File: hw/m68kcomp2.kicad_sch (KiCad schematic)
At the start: 61 parts, among them U10 as6c8008, U11 mc68681, U12 as6c8008, U13 mc1489, U14 mc1488, U15 mc1488, U16 as6c8008, U17 sera, U18 serb, U2 74HC393, U3 74HC10, U4 74HC148, U5 mc68030rc, U6 28C256, U7 mc68881, U8 as6c8008, U9 GAL16V8, X1 25.175MHz, Y1 3.6864MHz

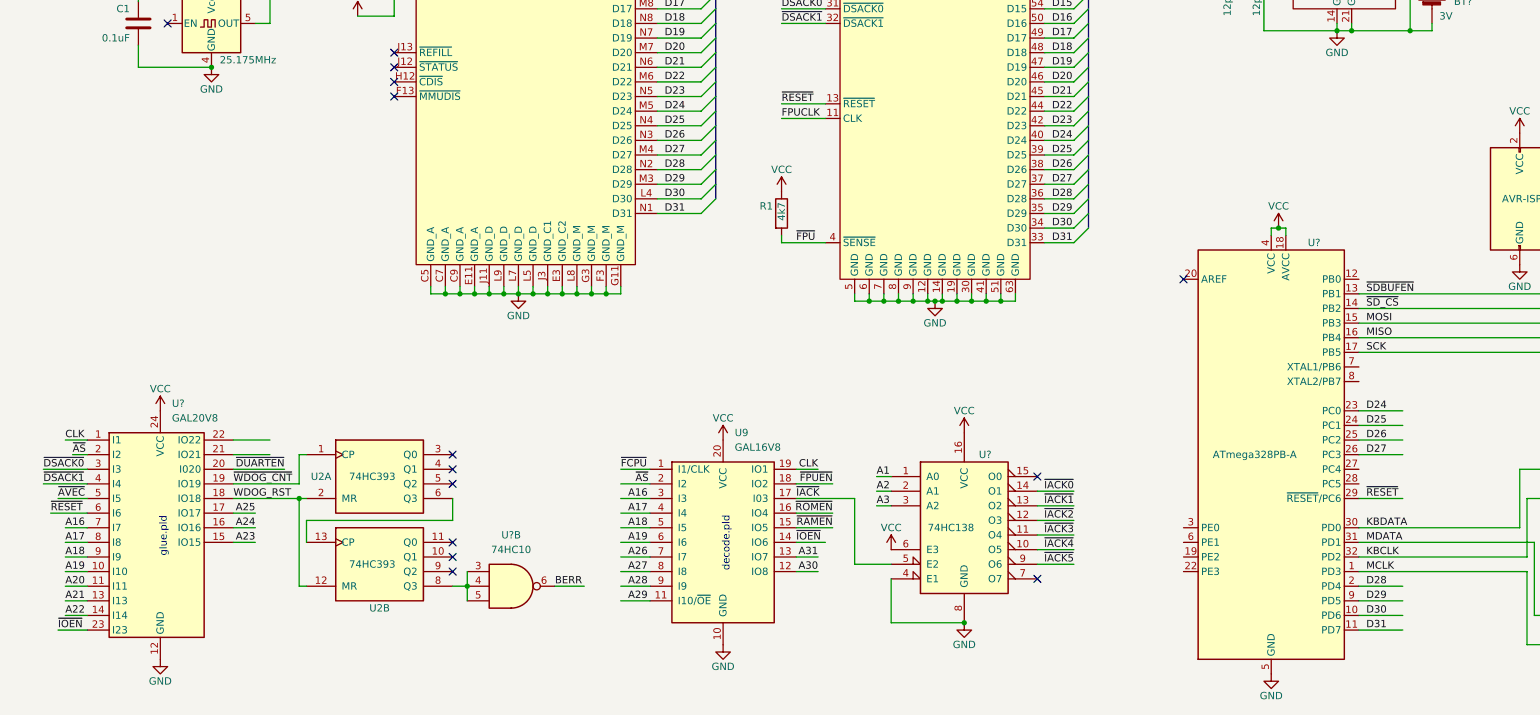
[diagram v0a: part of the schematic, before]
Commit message: schematic progress, split iodecode from glue.pld...
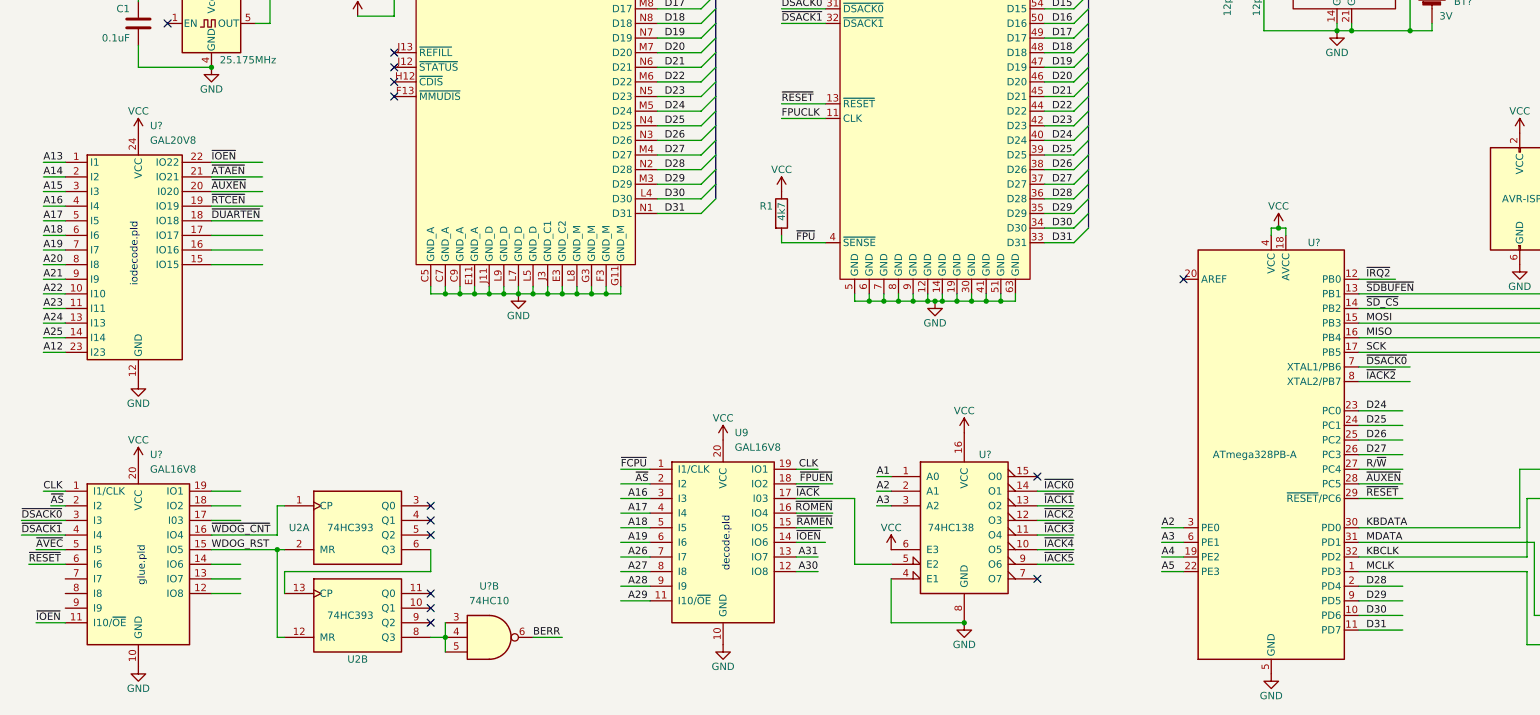
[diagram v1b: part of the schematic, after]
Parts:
- removed U?: GAL20V8, symbol m68kcomp2:GAL20V8
- added U?: GAL20V8, symbol m68kcomp2:GAL20V8
- added U?: GAL16V8, Package_DIP:DIP-20_W7.62mm_Socket, symbol Logic_Programmable:GAL16V8
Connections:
- net A12: now also U?.23 (I23)
- net A13: now also U?.1 (I1)
- net A14: now also U?.2 (I2)
- net A15: now also U?.3 (I3)
- net A16: now also U?.4 (I4)
- net A17: now also U?.5 (I5)
- net A18: now also U?.6 (I6)
- net A19: now also U?.7 (I7)
- net A2: now also U?.3 (PE0)
- net A20: now also U?.8 (I8)
- net A21: now also U?.9 (I9)
- net A22: now also U?.10 (I10)
- net A23: now also U?.11 (I11)
- net A24: now also U?.13 (I13)
- net A25: now also U?.14 (I14)
- net A3: now also U?.6 (PE1)
- net A4: now also U?.19 (PE2)
- net A5: now also U?.22 (PE3)
- net CLK: now also U?.1 (I1/CLK)
- net GND: now also U?.10 (GND), U?.12 (GND)
- net R/~{W}: now also U?.27 (PC4)
- net VCC: now also U?.20 (VCC), U?.24 (VCC)
- net WDOG_RST: now also U?.15 (IO5)
- net ~{AS}: now also U?.2 (I2)
- net ~{AVEC}: now also U?.5 (I5)
- net ~{DSACK0}: now also U?.7 (XTAL1/PB6), U?.3 (I3)
- net ~{DSACK1}: now also U?.4 (I4)
- net ~{DUARTEN}: now also U?.18 (IO18)
- net ~{IACK2}: now also U?.8 (XTAL2/PB7)
- net ~{IOEN}: now also U?.11 (I10/~{OE}), U?.22 (IO22)
- net ~{IRQ2}: now also U?.12 (PB0)
- net ~{RESET}: now also U?.6 (I6)
- net ~{RTCEN}: now also U?.19 (IO19)
- net ~{WDOG_CNT}: now also U?.16 (IO4)
- net ~{AUXEN}: now reaches U?.28 (PC5)
- net ~{AUXEN}: now also U?.20 (I020)
- new net ~{ATAEN}: U?.21 (IO21)
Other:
- note added: "iodecode.pld"
- moved on the sheet: U2A, U2B, U?B

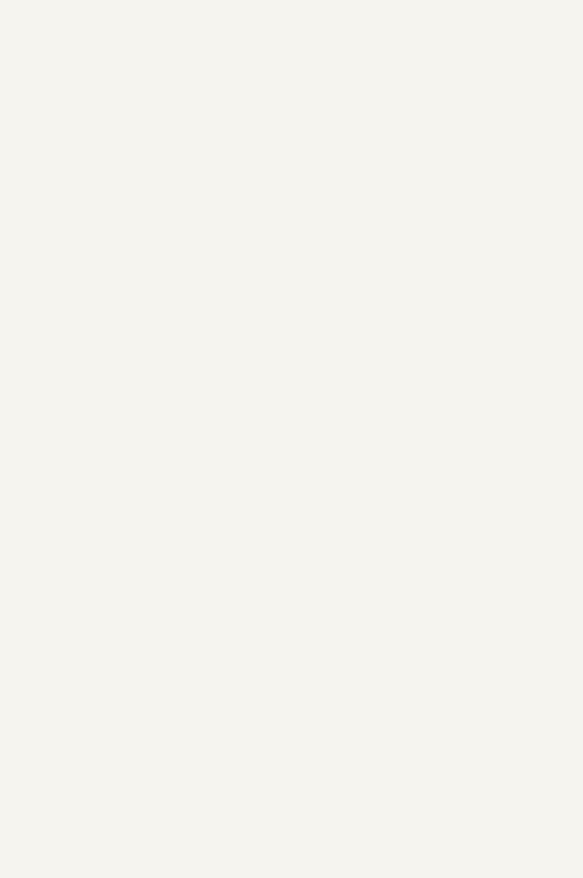
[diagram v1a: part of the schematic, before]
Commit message: ATA connector
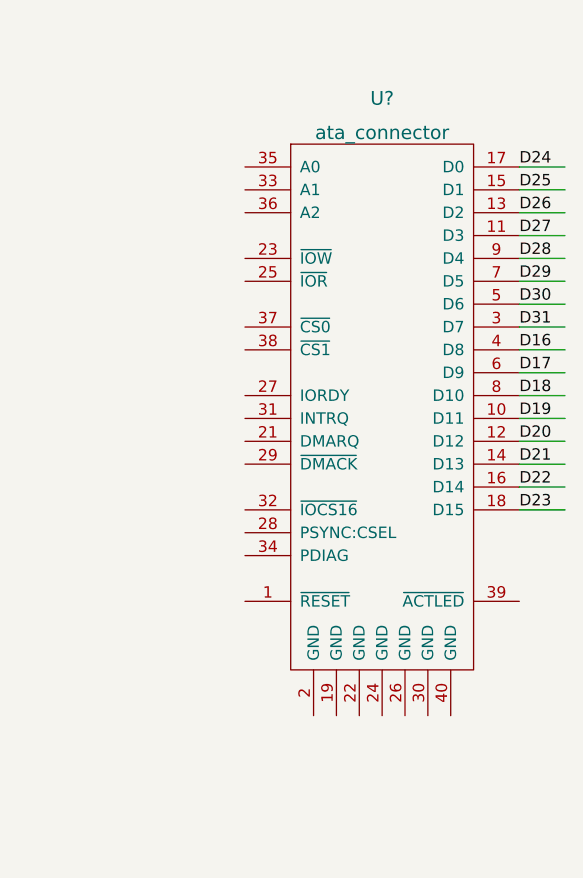
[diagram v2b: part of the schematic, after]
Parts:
- added U?: ata_connector, symbol m68kcomp2:ata_connector
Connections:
- net D16: now also U?.4 (D8)
- net D17: now also U?.6 (D9)
- net D18: now also U?.8 (D10)
- net D19: now also U?.10 (D11)
- net D20: now also U?.12 (D12)
- net D21: now also U?.14 (D13)
- net D22: now also U?.16 (D14)
- net D23: now also U?.18 (D15)
- net D24: now also U?.17 (D0)
- net D25: now also U?.15 (D1)
- net D26: now also U?.13 (D2)
- net D27: now also U?.11 (D3)
- net D28: now also U?.9 (D4)
- net D29: now also U?.7 (D5)
- net D30: now also U?.5 (D6)
- net D31: now also U?.3 (D7)

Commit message: broken up into multiple sheets, and added IOWAIT input to the watchdog
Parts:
- removed BT?: 3V, symbol Device:Battery_Cell
- removed C2, C3, C? (x2): 12pF, Capacitor_SMD:C_0805_2012Metric_Pad1.18x1.45mm_HandSolder, symbol Device:C_Small
- removed C?: 22uF, symbol Device:C_Polarized
- removed C?: 10uF, symbol Device:C_Polarized
- removed J?: AVR-ISP, symbol Connector:AVR-ISP-6
- removed U10, U12, U16, U8: as6c8008, Package_SO:TSOP-II-44_10.16x18.41mm_P0.8mm, symbol m68kcomp2:as6c8008
- removed U11: mc68681, Package_DIP:DIP-40_W15.24mm_Socket, symbol m68kcomp2:mc68681
- removed U13: mc1489, Package_SO:SO-14_3.9x8.65mm_P1.27mm, symbol m68kcomp2:mc1489
- removed U14, U15: mc1488, Package_SO:SO-14_3.9x8.65mm_P1.27mm, symbol m68kcomp2:mc1488
- removed U17: sera, Connector_Dsub:DSUB-9_Male_Horizontal_P2.77x2.54mm_EdgePinOffset9.40mm, symbol m68kcomp2:rs232_conn
- removed U18: serb, Connector_Dsub:DSUB-9_Male_Horizontal_P2.77x2.54mm_EdgePinOffset9.40mm, symbol m68kcomp2:rs232_conn
- removed U6: 28C256, Package_DIP:DIP-28_W15.24mm_Socket, symbol Memory_EEPROM:28C256
- removed U?: ds1501, symbol m68kcomp2:ds1501
- removed U? (x5): 74LVC125, symbol 74xx:74LVC125
- removed U?: LM1117-3.3, symbol Regulator_Linear:LM1117-3.3
- removed U?: mouse, symbol m68kcomp2:ps2conn
- removed U?: kbd, symbol m68kcomp2:ps2conn
- removed U?: ata_connector, symbol m68kcomp2:ata_connector
- removed U?: sdcard, symbol m68kcomp2:sdcard
- removed U?: ATmega328PB-A, Package_QFP:TQFP-32_7x7mm_P0.8mm, symbol MCU_Microchip_ATmega:ATmega328PB-A
- removed Y1: 3.6864MHz, Crystal:Crystal_SMD_ECS_CSM3X-2Pin_7.6x4.1mm, symbol Device:Crystal_Small
- removed Y?: 32.768kHz, Crystal:Crystal_SMD_ECS_CSM3X-2Pin_7.6x4.1mm, symbol Device:Crystal_Small
- added D?: 1N4148, Diode_THT:D_DO-35_SOD27_P7.62mm_Horizontal, symbol Diode:1N4148
- added R?: 4k7, OptoDevice:R_LDR_D13.8mm_P9.0mm_Vertical, symbol Device:R
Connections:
- net VCC: now also R?.1
- net ~{AUXEN}: now also D?.1 (K)
- net ~{IOWAIT}: now reaches U?.9 (I9)
- net ~{IOWAIT}: now also D?.2 (A), R?.2
- no-connect marks 48 -> 26
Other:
- added sheet io (io.kicad_sch)
- added sheet memory (memory.kicad_sch)
- moved on the sheet: C1, C?, D?, J?, JP?, R1, R?, RN1, SW?, U2A, U2B, U3A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

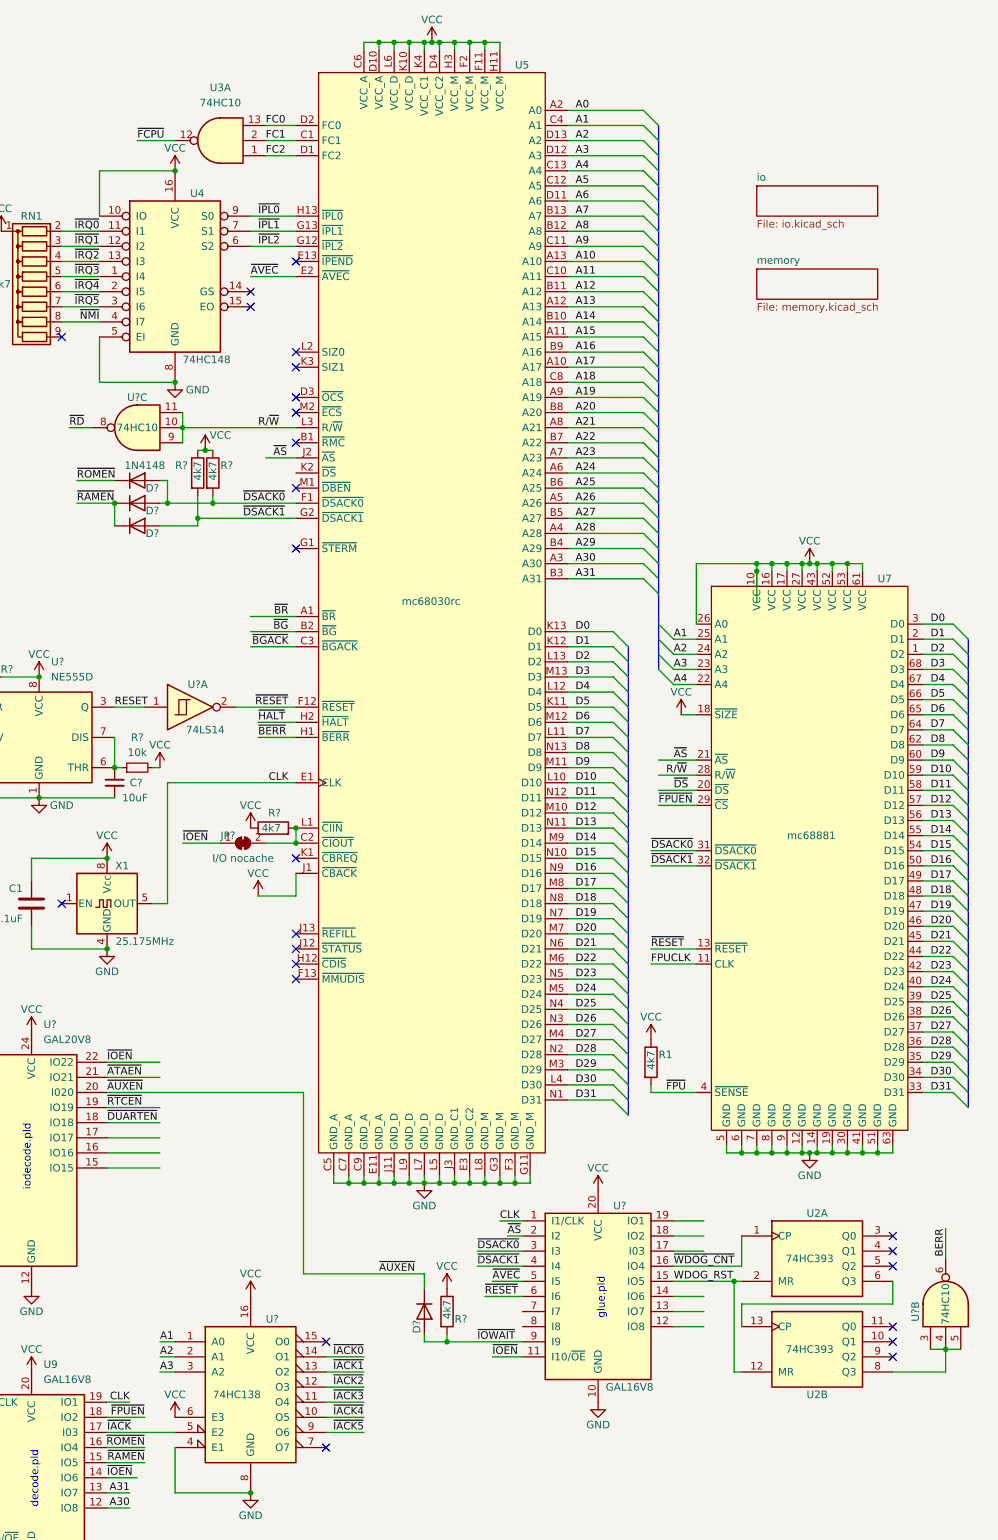
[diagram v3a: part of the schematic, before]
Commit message: expansion, compactflash connector, 3v3reg jumper
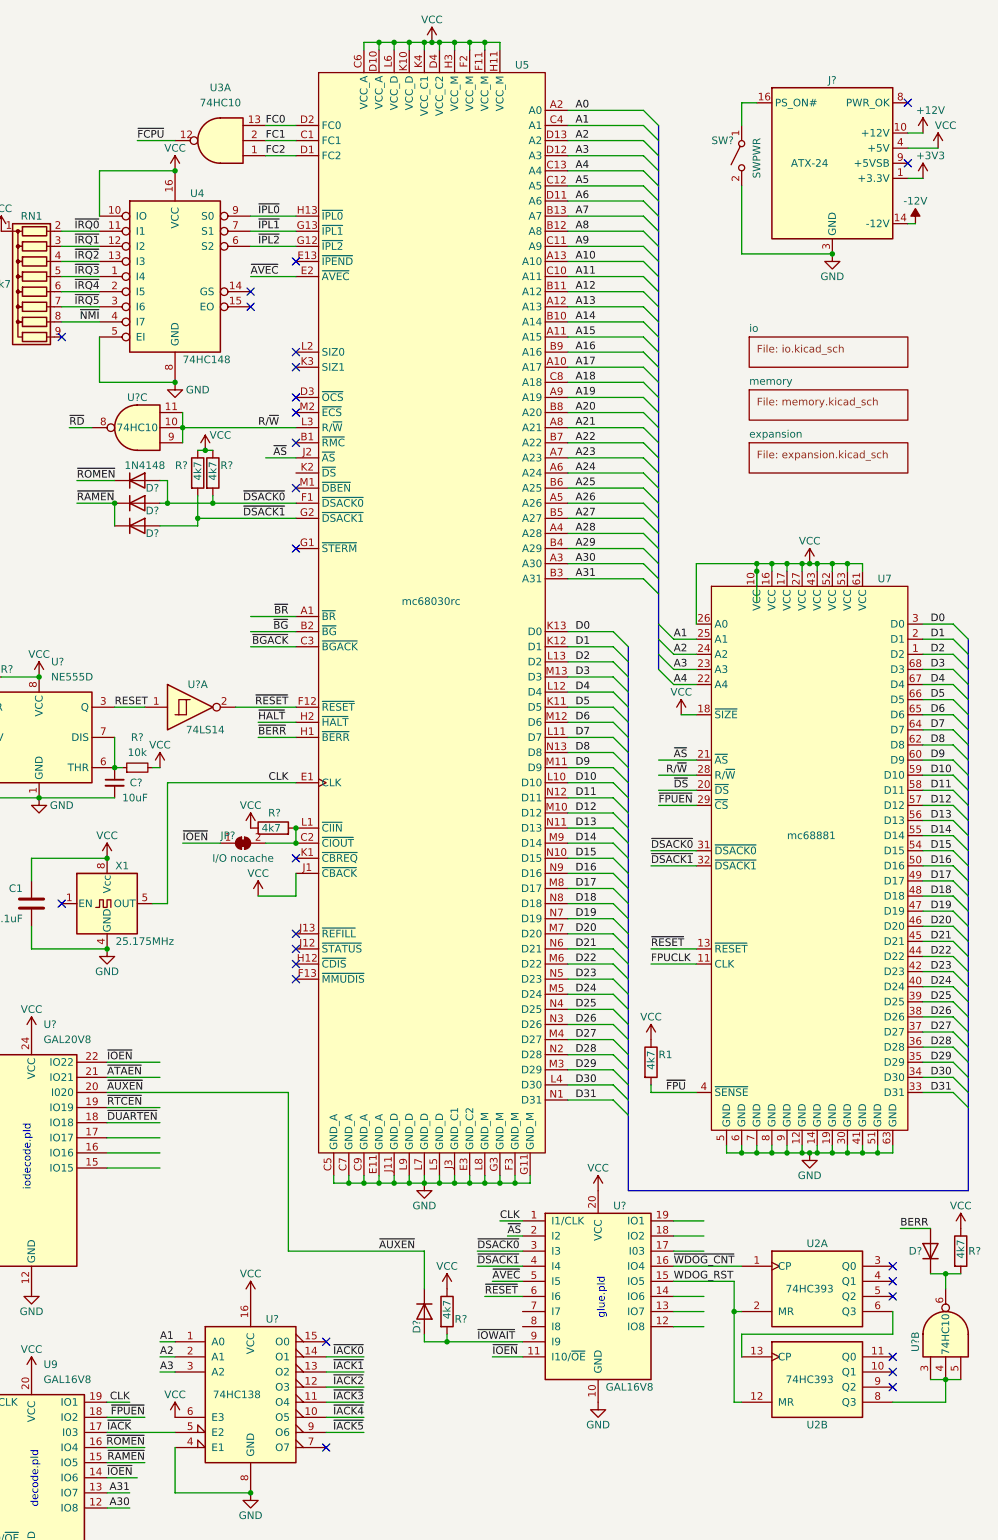
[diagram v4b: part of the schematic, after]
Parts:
- added D?: 1N4148, Diode_THT:D_DO-35_SOD27_P7.62mm_Horizontal, symbol Diode:1N4148
- added J?: ATX-24, symbol Connector:ATX-24
- added R?: 4k7, OptoDevice:R_LDR_D13.8mm_P9.0mm_Vertical, symbol Device:R
- added SW?: SWPWR, symbol Switch:SW_SPST
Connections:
- net BERR: now also D?.2 (A); no longer U?.6
- net GND: now also J?.15 (GND), J?.17 (GND), J?.18 (GND), J?.19 (GND), J?.24 (GND), J?.3 (GND), J?.5 (GND), J?.7 (GND), SW?.2 (B)
- net VCC: now also J?.21 (+5V), J?.22 (+5V), J?.23 (+5V), J?.4 (+5V), J?.6 (+5V), R?.1
- new net: D?.1 (K), R?.2, U?.6
- new net: J?.16 (PS_ON#), SW?.1 (A)
- new net +12V: J?.10 (+12V), J?.11 (+12V)
- new net +3V3: J?.1 (+3.3V), J?.12 (+3.3V), J?.13 (+3.3V), J?.2 (+3.3V)
- new net -12V: J?.14 (-12V)
- no-connect marks 26 -> 28
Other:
- added sheet expansion (expansion.kicad_sch)
- moved on the sheet: U2A, U2B, U?B
